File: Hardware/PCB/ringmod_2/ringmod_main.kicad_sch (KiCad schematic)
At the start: 61 parts, among them J1 Synth_power_2x5, J2 AudioJack2, J3 AudioJack2, J4 AudioJack2, J5 AudioJack2, J9 AudioJack2, U1 NE5532, U2 TL071, U3 TL072

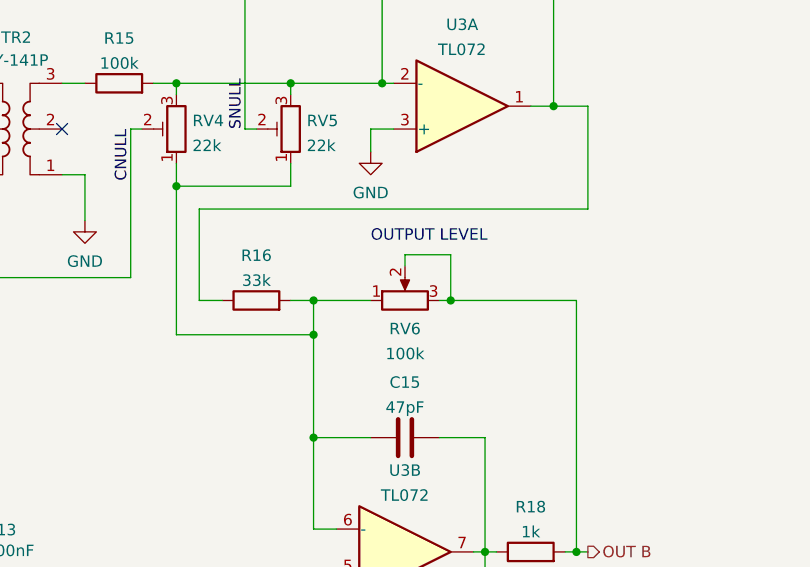
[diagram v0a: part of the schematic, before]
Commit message: Update pot symbols
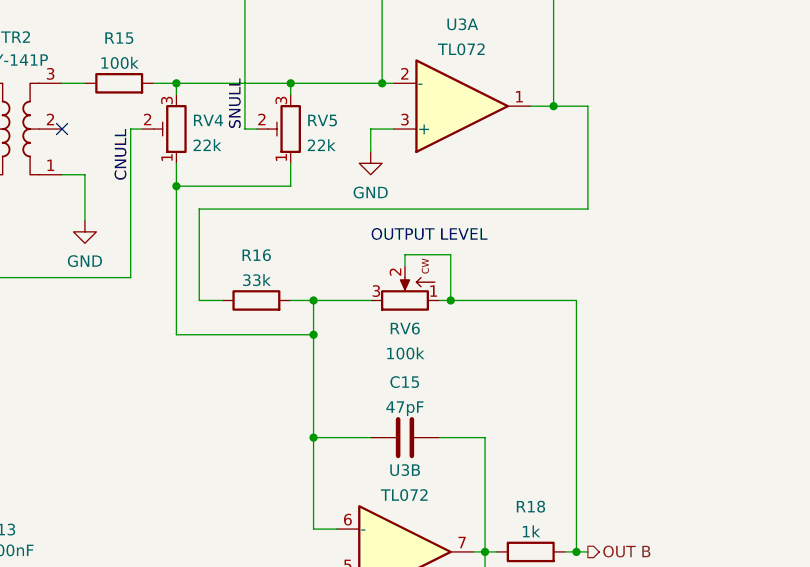
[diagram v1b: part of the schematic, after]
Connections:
- net OUT B: now also RV6.1; no longer RV6.3
- net at C15.1, R16.2, RV4.1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: now also RV6.3; no longer RV6.1
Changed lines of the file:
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@@
     (comment 3 "Circuit design by Ken Stone.")
   )
-  (junction (at 214.63 86.36) (diameter 0) (color 0 0 0 0))
+  (junction (at 152.4 58.42) (diameter 0) (color 0 0 0 0))
+  (junction (at 81.28 157.48) (diameter 0) (color 0 0 0 0))
+  (junction (at 147.32 58.42) (diameter 0) (color 0 0 0 0))
+  (junction (at 157.48 95.25) (diameter 0) (color 0 0 0 0))
   (junction (at 85.09 90.17) (diameter 0) (color 0 0 0 0))
+  (junction (at 83.82 58.42) (diameter 0) (color 0 0 0 0))
+  (junction (at 119.38 152.4) (diameter 0) (color 0 0 0 0))
+  (junction (at 119.38 160.02) (diameter 0) (color 0 0 0 0))
+  (junction (at 142.24 160.02) (diameter 0) (color 0 0 0 0))
+  (junction (at 226.06 149.86) (diameter 0) (color 0 0 0 0))
+  (junction (at 157.48 110.49) (diameter 0) (color 0 0 0 0))
+  (junction (at 233.68 100.33) (diameter 0) (color 0 0 0 0))
+  (junction (at 118.11 55.88) (diameter 0) (color 0 0 0 0))
+  (junction (at 133.35 119.38) (diameter 0) (color 0 0 0 0))
+  (junction (at 87.63 41.91) (diameter 0) (color 0 0 0 0))
+  (junction (at 191.77 109.22) (diameter 0) (color 0 0 0 0))
+  (junction (at 85.09 105.41) (diameter 0) (color 0 0 0 0))
   (junction (at 207.01 137.16) (diameter 0) (color 0 0 0 0))
+  (junction (at 142.24 152.4) (diameter 0) (color 0 0 0 0))
+  (junction (at 55.88 157.48) (diameter 0) (color 0 0 0 0))
   (junction (at 33.02 152.4) (diameter 0) (color 0 0 0 0))
-  (junction (at 81.28 157.48) (diameter 0) (color 0 0 0 0))
-  (junction (at 157.48 95.25) (diameter 0) (color 0 0 0 0))
-  (junction (at 87.63 41.91) (diameter 0) (color 0 0 0 0))
-  (junction (at 85.09 116.84) (diameter 0) (color 0 0 0 0))
-  (junction (at 167.64 152.4) (diameter 0) (color 0 0 0 0))
+  (junction (at 207.01 125.73) (diameter 0) (color 0 0 0 0))
+  (junction (at 118.11 45.72) (diameter 0) (color 0 0 0 0))
   (junction (at 104.14 119.38) (diameter 0) (color 0 0 0 0))
-  (junction (at 236.22 149.86) (diameter 0) (color 0 0 0 0))
-  (junction (at 106.68 63.5) (diameter 0) (color 0 0 0 0))
-  (junction (at 142.24 160.02) (diameter 0) (color 0 0 0 0))
-  (junction (at 55.88 147.32) (diameter 0) (color 0 0 0 0))
-  (junction (at 222.25 121.92) (diameter 0) (color 0 0 0 0))
-  (junction (at 207.01 125.73) (diameter 0) (color 0 0 0 0))
-  (junction (at 142.24 95.25) (diameter 0) (color 0 0 0 0))
-  (junction (at 118.11 45.72) (diameter 0) (color 0 0 0 0))
-  (junction (at 85.09 105.41) (diameter 0) (color 0 0 0 0))
-  (junction (at 85.09 99.06) (diameter 0) (color 0 0 0 0))
-  (junction (at 204.47 97.79) (diameter 0) (color 0 0 0 0))
-  (junction (at 147.32 58.42) (diameter 0) (color 0 0 0 0))
-  (junction (at 137.16 58.42) (diameter 0) (color 0 0 0 0))
   (junction (at 102.87 152.4) (diameter 0) (color 0 0 0 0))
-  (junction (at 142.24 144.78) (diameter 0) (color 0 0 0 0))
-  (junction (at 114.3 119.38) (diameter 0) (color 0 0 0 0))
-  (junction (at 119.38 160.02) (diameter 0) (color 0 0 0 0))
-  (junction (at 142.24 110.49) (diameter 0) (color 0 0 0 0))
   (junction (at 214.63 97.79) (diameter 0) (color 0 0 0 0))
-  (junction (at 207.01 121.92) (diameter 0) (color 0 0 0 0))
-  (junction (at 152.4 58.42) (diameter 0) (color 0 0 0 0))
-  (junction (at 142.24 152.4) (diameter 0) (color 0 0 0 0))
-  (junction (at 133.35 119.38) (diameter 0) (color 0 0 0 0))
-  (junction (at 118.11 30.48) (diameter 0) (color 0 0 0 0))
-  (junction (at 106.68 55.88) (diameter 0) (color 0 0 0 0))
-  (junction (at 62.23 99.06) (diameter 0) (color 0 0 0 0))
-  (junction (at 76.2 58.42) (diameter 0) (color 0 0 0 0))
   (junction (at 81.28 147.32) (diameter 0) (color 0 0 0 0))
   (junction (at 233.68 86.36) (diameter 0) (color 0 0 0 0))
-  (junction (at 55.88 157.48) (diameter 0) (color 0 0 0 0))
-  (junction (at 119.38 152.4) (diameter 0) (color 0 0 0 0))
-  (junction (at 157.48 110.49) (diameter 0) (color 0 0 0 0))
-  (junction (at 226.06 149.86) (diameter 0) (color 0 0 0 0))
-  (junction (at 83.82 58.42) (diameter 0) (color 0 0 0 0))
+  (junction (at 191.77 97.79) (diameter 0) (color 0 0 0 0))
+  (junction (at 236.22 149.86) (diameter 0) (color 0 0 0 0))
+  (junction (at 214.63 86.36) (diameter 0) (color 0 0 0 0))
+  (junction (at 85.09 99.06) (diameter 0) (color 0 0 0 0))
+  (junction (at 207.01 121.92) (diameter 0) (color 0 0 0 0))
+  (junction (at 119.38 144.78) (diameter 0) (color 0 0 0 0))
+  (junction (at 62.23 99.06) (diameter 0) (color 0 0 0 0))
   (junction (at 55.88 152.4) (diameter 0) (color 0 0 0 0))
+  (junction (at 142.24 110.49) (diameter 0) (color 0 0 0 0))
+  (junction (at 167.64 152.4) (diameter 0) (color 0 0 0 0))
+  (junction (at 106.68 55.88) (diameter 0) (color 0 0 0 0))
+  (junction (at 222.25 121.92) (diameter 0) (color 0 0 0 0))
+  (junction (at 118.11 30.48) (diameter 0) (color 0 0 0 0))
+  (junction (at 106.68 63.5) (diameter 0) (color 0 0 0 0))
+  (junction (at 55.88 147.32) (diameter 0) (color 0 0 0 0))
+  (junction (at 204.47 97.79) (diameter 0) (color 0 0 0 0))
+  (junction (at 85.09 116.84) (diameter 0) (color 0 0 0 0))
+  (junction (at 114.3 119.38) (diameter 0) (color 0 0 0 0))
+  (junction (at 142.24 144.78) (diameter 0) (color 0 0 0 0))
+  (junction (at 137.16 58.42) (diameter 0) (color 0 0 0 0))
+  (junction (at 142.24 95.25) (diameter 0) (color 0 0 0 0))
+  (junction (at 76.2 58.42) (diameter 0) (color 0 0 0 0))
   (junction (at 106.68 41.91) (diameter 0) (color 0 0 0 0))
-  (junction (at 191.77 109.22) (diameter 0) (color 0 0 0 0))
-  (junction (at 233.68 100.33) (diameter 0) (color 0 0 0 0))
   (junction (at 63.5 58.42) (diameter 0) (color 0 0 0 0))
-  (junction (at 118.11 55.88) (diameter 0) (color 0 0 0 0))
-  (junction (at 119.38 144.78) (diameter 0) (color 0 0 0 0))
-  (junction (at 191.77 97.79) (diameter 0) (color 0 0 0 0))
   (no_connect (at 96.52 48.26))
   (no_connect (at 99.06 48.26))

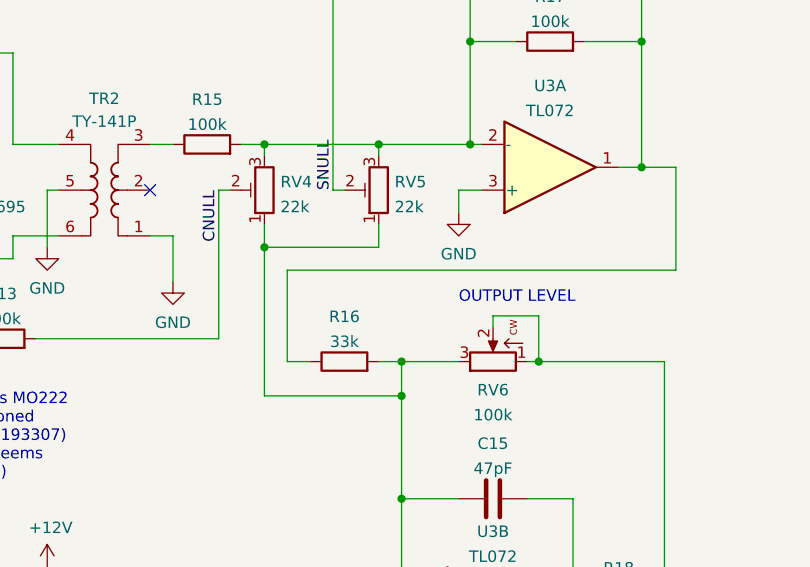
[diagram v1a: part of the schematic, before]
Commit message: .gitignore, fix pot symbols
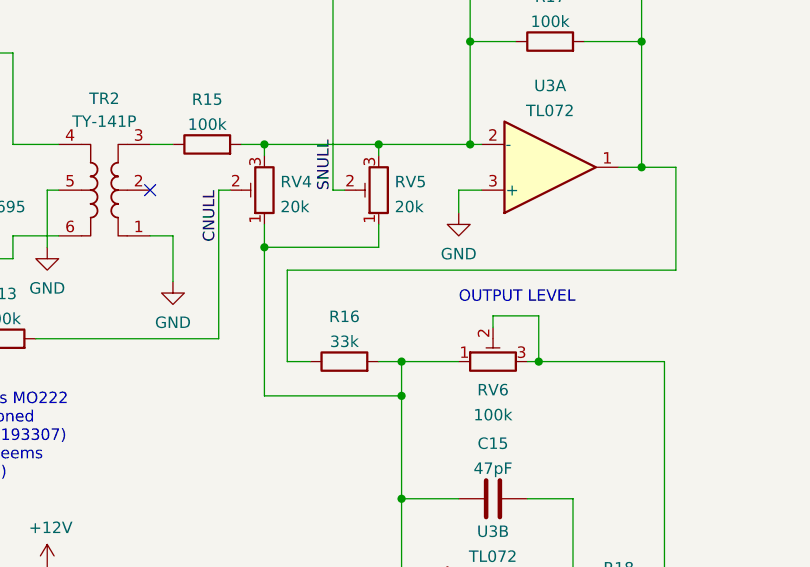
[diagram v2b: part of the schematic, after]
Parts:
- RV4, RV5: value 22k -> 20k
- RV6: symbol ao_symbols:R_POT -> ao_symbols:R_POT_TRIM_3296W
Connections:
- net OUT B: now also RV6.3; no longer RV6.1
- net at C15.1, R16.2, RV4.1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: now also RV6.1; no longer RV6.3
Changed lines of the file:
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@@
-(kicad_sch (version 20210621) (generator eeschema)
+(kicad_sch (version 20211123) (generator eeschema)
   (paper "USLetter")
   (title_block
@@
     (comment 3 "Circuit design by Ken Stone.")
   )
-  (junction (at 152.4 58.42) (diameter 0) (color 0 0 0 0))
-  (junction (at 81.28 157.48) (diameter 0) (color 0 0 0 0))
-  (junction (at 147.32 58.42) (diameter 0) (color 0 0 0 0))
-  (junction (at 157.48 95.25) (diameter 0) (color 0 0 0 0))
-  (junction (at 85.09 90.17) (diameter 0) (color 0 0 0 0))
-  (junction (at 83.82 58.42) (diameter 0) (color 0 0 0 0))
-  (junction (at 119.38 152.4) (diameter 0) (color 0 0 0 0))
-  (junction (at 119.38 160.02) (diameter 0) (color 0 0 0 0))
-  (junction (at 142.24 160.02) (diameter 0) (color 0 0 0 0))
-  (junction (at 226.06 149.86) (diameter 0) (color 0 0 0 0))
-  (junction (at 157.48 110.49) (diameter 0) (color 0 0 0 0))
-  (junction (at 233.68 100.33) (diameter 0) (color 0 0 0 0))
-  (junction (at 118.11 55.88) (diameter 0) (color 0 0 0 0))
-  (junction (at 133.35 119.38) (diameter 0) (color 0 0 0 0))
-  (junction (at 87.63 41.91) (diameter 0) (color 0 0 0 0))
-  (junction (at 191.77 109.22) (diameter 0) (color 0 0 0 0))
-  (junction (at 85.09 105.41) (diameter 0) (color 0 0 0 0))
-  (junction (at 207.01 137.16) (diameter 0) (color 0 0 0 0))
-  (junction (at 142.24 152.4) (diameter 0) (color 0 0 0 0))
-  (junction (at 55.88 157.48) (diameter 0) (color 0 0 0 0))
-  (junction (at 33.02 152.4) (diameter 0) (color 0 0 0 0))
-  (junction (at 207.01 125.73) (diameter 0) (color 0 0 0 0))
-  (junction (at 118.11 45.72) (diameter 0) (color 0 0 0 0))
-  (junction (at 104.14 119.38) (diameter 0) (color 0 0 0 0))
-  (junction (at 102.87 152.4) (diameter 0) (color 0 0 0 0))
-  (junction (at 214.63 97.79) (diameter 0) (color 0 0 0 0))
-  (junction (at 81.28 147.32) (diameter 0) (color 0 0 0 0))
-  (junction (at 233.68 86.36) (diameter 0) (color 0 0 0 0))
-  (junction (at 191.77 97.79) (diameter 0) (color 0 0 0 0))
-  (junction (at 236.22 149.86) (diameter 0) (color 0 0 0 0))
-  (junction (at 214.63 86.36) (diameter 0) (color 0 0 0 0))
-  (junction (at 85.09 99.06) (diameter 0) (color 0 0 0 0))
-  (junction (at 207.01 121.92) (diameter 0) (color 0 0 0 0))
-  (junction (at 119.38 144.78) (diameter 0) (color 0 0 0 0))
-  (junction (at 62.23 99.06) (diameter 0) (color 0 0 0 0))
-  (junction (at 55.88 152.4) (diameter 0) (color 0 0 0 0))
-  (junction (at 142.24 110.49) (diameter 0) (color 0 0 0 0))
-  (junction (at 167.64 152.4) (diameter 0) (color 0 0 0 0))
-  (junction (at 106.68 55.88) (diameter 0) (color 0 0 0 0))
-  (junction (at 222.25 121.92) (diameter 0) (color 0 0 0 0))
-  (junction (at 118.11 30.48) (diameter 0) (color 0 0 0 0))
-  (junction (at 106.68 63.5) (diameter 0) (color 0 0 0 0))
-  (junction (at 55.88 147.32) (diameter 0) (color 0 0 0 0))
-  (junction (at 204.47 97.79) (diameter 0) (color 0 0 0 0))
-  (junction (at 85.09 116.84) (diameter 0) (color 0 0 0 0))
-  (junction (at 114.3 119.38) (diameter 0) (color 0 0 0 0))
-  (junction (at 142.24 144.78) (diameter 0) (color 0 0 0 0))
-  (junction (at 137.16 58.42) (diameter 0) (color 0 0 0 0))
-  (junction (at 142.24 95.25) (diameter 0) (color 0 0 0 0))
-  (junction (at 76.2 58.42) (diameter 0) (color 0 0 0 0))
-  (junction (at 106.68 41.91) (diameter 0) (color 0 0 0 0))
-  (junction (at 63.5 58.42) (diameter 0) (color 0 0 0 0))
+  (junction (at 207.01 121.92) (diameter 0) (color 0 0 0 0)
+  )
+  (junction (at 207.01 137.16) (diameter 0) (color 0 0 0 0)
+  )
+  (junction (at 119.38 160.02) (diameter 0) (color 0 0 0 0)
+  )
+  (junction (at 76.2 58.42) (diameter 0) (color 0 0 0 0)
+  )
+  (junction (at 102.87 152.4) (diameter 0) (color 0 0 0 0)
+  )
+  (junction (at 62.23 99.06) (diameter 0) (color 0 0 0 0)
+  )
+  (junction (at 85.09 90.17) (diameter 0) (color 0 0 0 0)
+  )
+  (junction (at 55.88 147.32) (diameter 0) (color 0 0 0 0)
+  )
+  (junction (at 204.47 97.79) (diameter 0) (color 0 0 0 0)
+  )
+  (junction (at 119.38 144.78) (diameter 0) (color 0 0 0 0)
+  )
+  (junction (at 191.77 97.79) (diameter 0) (color 0 0 0 0)
+  )
+  (junction (at 118.11 45.72) (diameter 0) (color 0 0 0 0)
+  )
+  (junction (at 137.16 58.42) (diameter 0) (color 0 0 0 0)
+  )
+  (junction (at 106.68 55.88) (diameter 0) (color 0 0 0 0)
+  )
+  (junction (at 152.4 58.42) (diameter 0) (color 0 0 0 0)
+  )
+  (junction (at 142.24 152.4) (diameter 0) (color 0 0 0 0)
+  )
+  (junction (at 83.82 58.42) (diameter 0) (color 0 0 0 0)
+  )
+  (junction (at 207.01 125.73) (diameter 0) (color 0 0 0 0)
+  )
+  (junction (at 106.68 63.5) (diameter 0) (color 0 0 0 0)
+  )
+  (junction (at 233.68 100.33) (diameter 0) (color 0 0 0 0)
+  )
+  (junction (at 147.32 58.42) (diameter 0) (color 0 0 0 0)
+  )
+  (junction (at 114.3 119.38) (diameter 0) (color 0 0 0 0)
+  )
+  (junction (at 55.88 152.4) (diameter 0) (color 0 0 0 0)
+  )
+  (junction (at 119.38 152.4) (diameter 0) (color 0 0 0 0)
+  )
+  (junction (at 214.63 86.36) (diameter 0) (color 0 0 0 0)
+  )
+  (junction (at 157.48 110.49) (diameter 0) (color 0 0 0 0)
+  )
+  (junction (at 142.24 160.02) (diameter 0) (color 0 0 0 0)
+  )
+  (junction (at 142.24 95.25) (diameter 0) (color 0 0 0 0)
+  )
+  (junction (at 236.22 149.86) (diameter 0) (color 0 0 0 0)
+  )
+  (junction (at 118.11 55.88) (diameter 0) (color 0 0 0 0)
+  )
+  (junction (at 226.06 149.86) (diameter 0) (color 0 0 0 0)
+  )
+  (junction (at 222.25 121.92) (diameter 0) (color 0 0 0 0)
+  )
+  (junction (at 85.09 105.41) (diameter 0) (color 0 0 0 0)
+  )
+  (junction (at 142.24 110.49) (diameter 0) (color 0 0 0 0)
+  )
+  (junction (at 81.28 157.48) (diameter 0) (color 0 0 0 0)
+  )
+  (junction (at 133.35 119.38) (diameter 0) (color 0 0 0 0)
+  )
+  (junction (at 87.63 41.91) (diameter 0) (color 0 0 0 0)
+  )
+  (junction (at 214.63 97.79) (diameter 0) (color 0 0 0 0)
+  )
+  (junction (at 81.28 147.32) (diameter 0) (color 0 0 0 0)
+  )
+  (junction (at 167.64 152.4) (diameter 0) (color 0 0 0 0)
+  )
+  (junction (at 106.68 41.91) (diameter 0) (color 0 0 0 0)
+  )
+  (junction (at 104.14 119.38) (diameter 0) (color 0 0 0 0)
+  )
+  (junction (at 142.24 144.78) (diameter 0) (color 0 0 0 0)
+  )
+  (junction (at 118.11 30.48) (diameter 0) (color 0 0 0 0)
+  )
+  (junction (at 85.09 99.06) (diameter 0) (color 0 0 0 0)
+  )
+  (junction (at 55.88 157.48) (diameter 0) (color 0 0 0 0)
+  )
+  (junction (at 63.5 58.42) (diameter 0) (color 0 0 0 0)
+  )
+  (junction (at 85.09 116.84) (diameter 0) (color 0 0 0 0)
+  )
+  (junction (at 157.48 95.25) (diameter 0) (color 0 0 0 0)
+  )
+  (junction (at 191.77 109.22) (diameter 0) (color 0 0 0 0)
+  )
+  (junction (at 233.68 86.36) (diameter 0) (color 0 0 0 0)
+  )
+  (junction (at 33.02 152.4) (diameter 0) (color 0 0 0 0)
+  )
   (no_connect (at 96.52 48.26))
   (no_connect (at 99.06 48.26))
@@
     (pin "1")
   )
-  (symbol (lib_id "ao_symbols:R_POT") (at 217.17 121.92 90) (unit 1)
+  (symbol (lib_id "ao_symbols:R_POT_TRIM_3296W") (at 217.17 121.92 90) (unit 1)
     (in_bom yes) (on_board yes) (fields_autoplaced)
     (property "Reference" "RV6" (id 0) (at 217.17 125.0855 90))
@@
       (effects (font (size 1.27 1.27)) (justify right))
     )
-    (property "Value" "22k" (id 1) (at 193.548 104.7366 0)
+    (property "Value" "20k" (id 1) (at 193.548 104.7366 0)
       (effects (font (size 1.27 1.27)) (justify right))
     )
@@
       (effects (font (size 1.27 1.27)) (justify right))
     )
-    (property "Value" "22k" (id 1) (at 206.248 104.7366 0)
+    (property "Value" "20k" (id 1) (at 206.248 104.7366 0)
       (effects (font (size 1.27 1.27)) (justify right))
     )
